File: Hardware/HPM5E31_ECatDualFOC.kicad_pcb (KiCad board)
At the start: 4 copper layers, 85 x 113.4 mm, 403 parts, among them J1 Conn_Coaxial, J11 PHB2.0-02-20PWZ, J12 PHB2.0-02-20PWZ, J13 RJ45_Hanrun_HR911105A_Horizon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, J14 RJ45_Hanrun_HR911105A_Horizon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, J15 WAFER-GH1.25-4PWB, J16 WAFER-GH1.25-4PWB, J17 WAFER-GH1.25-4PWB, J18 WAFER-GH1.25-2PWB, J19 WAFER-GH1.25-2PWB, J2 WAFER-ZH1.5-4PWB, J20 Conn_Coaxial, J3 Conn_02x05_Odd_Even, J4 USB_B, K1 DSHP02TSGET, Q1 CSD19532Q5B, Q10 CSD19532Q5B, Q11 CSD19532Q5B, Q12 CSD19532Q5B, Q13 NCE01ND03S, Q14 NCE01ND03S, Q15 SI2305, Q16 SI2305, Q17 SS8050, Q18 SS8050, Q2 CSD19532Q5B, Q3 CSD19532Q5B, Q4 CSD19532Q5B, Q5 CSD19532Q5B, Q6 CSD19532Q5B, Q7 CSD19532Q5B, Q8 CSD19532Q5B, Q9 CSD19532Q5B, U1 HPM5E31IGN1, U10 UCC27282DRCR, U11 INA240A1PWR, U12 UCC27282DRCR, U13 INA240A1PWR, U14 UCC27282DRCR, U15 INA240A1PWR, U16 INA240A1PWR, U17 UCC27282DRCR, U18 INA240A1PWR, U19 UCC27282DRCR, U2 LM5164DDAR, U20 INA240A1PWR, U21 UCC27282DRCR, U22 INA240A1PWR, U23 INA240A1PWR, U24 PY32F002BF15U, U25 EG2104, U26 ZX-HY2.0-2PWT, U27 RT9193-33GB-MS, U28 EG2104, U29 ZX-HY2.0-2PWT, U3 MP1605GTF-Z, U30 RS622XTDE8, U31 MS2575T, U32 TXB0104RUTR, U33 MS2575T, U34 M3, U35 MS2575T, U36 TXB0104RUTR, U37 MS2575T, U38 M3, U39 JL1111-N032I, U40 JL1111-N032I, U41 SP3485EN-L/TR, U42 SP3485EN-L/TR, U43 SP3485EN-L/TR, U44 TJA1042TK/3, U45 TJA1042TK/3, U46 M3, U47 M3, U5 JW5026, U6 MP1605GTF-Z, U7 LP5907MFX-3.3/NOPB, U8 REF3030AIDBZR, U9 MX25L12833FM2I-10G, X1 24M,10ppm

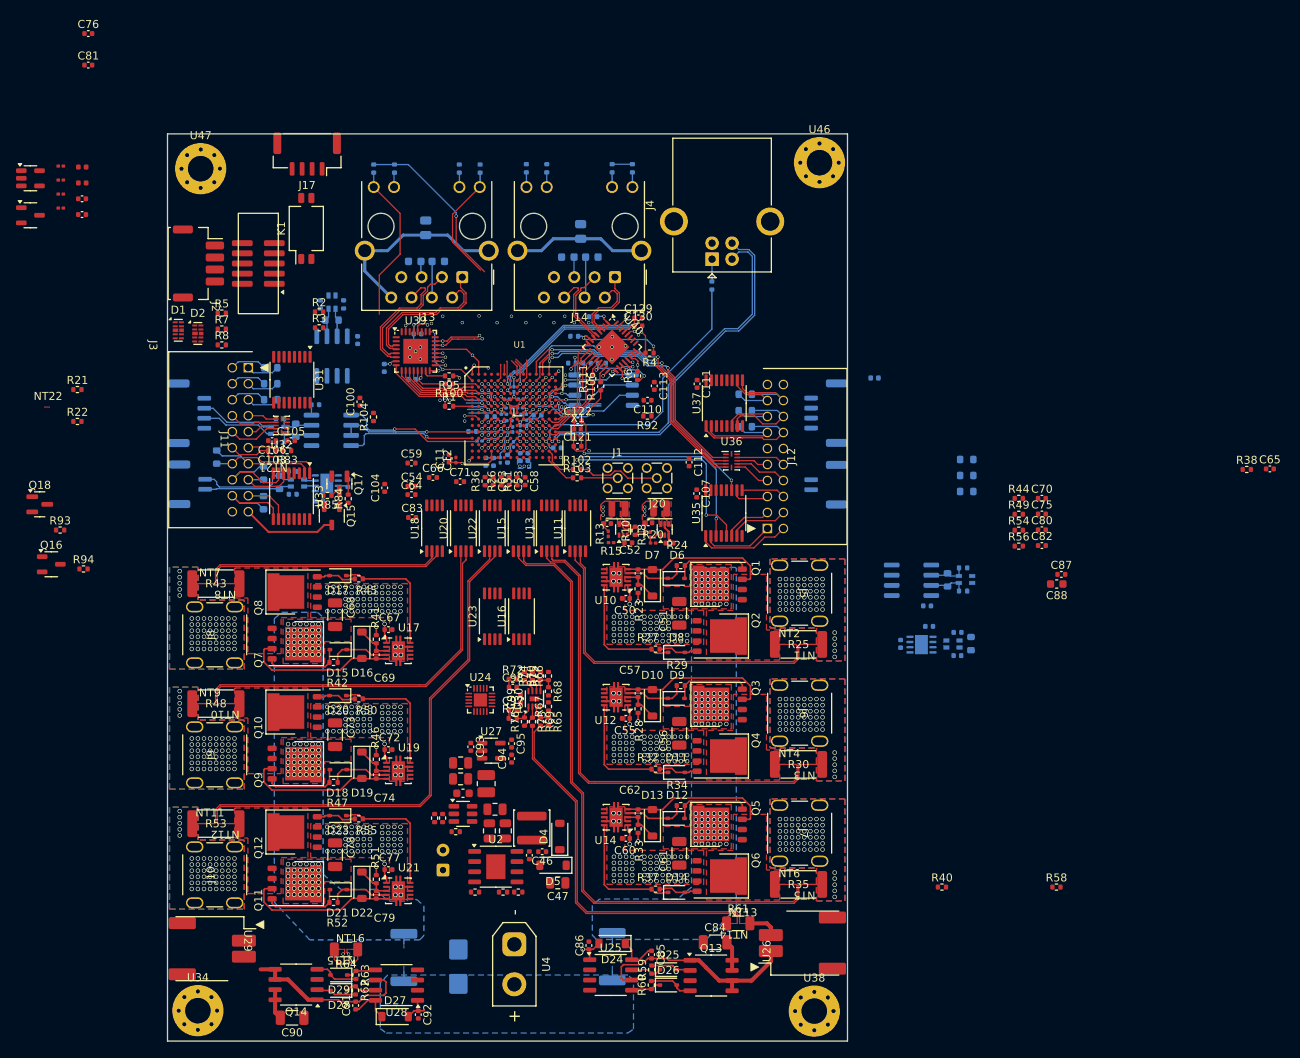
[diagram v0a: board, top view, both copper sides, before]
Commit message: 调整引脚，拉线
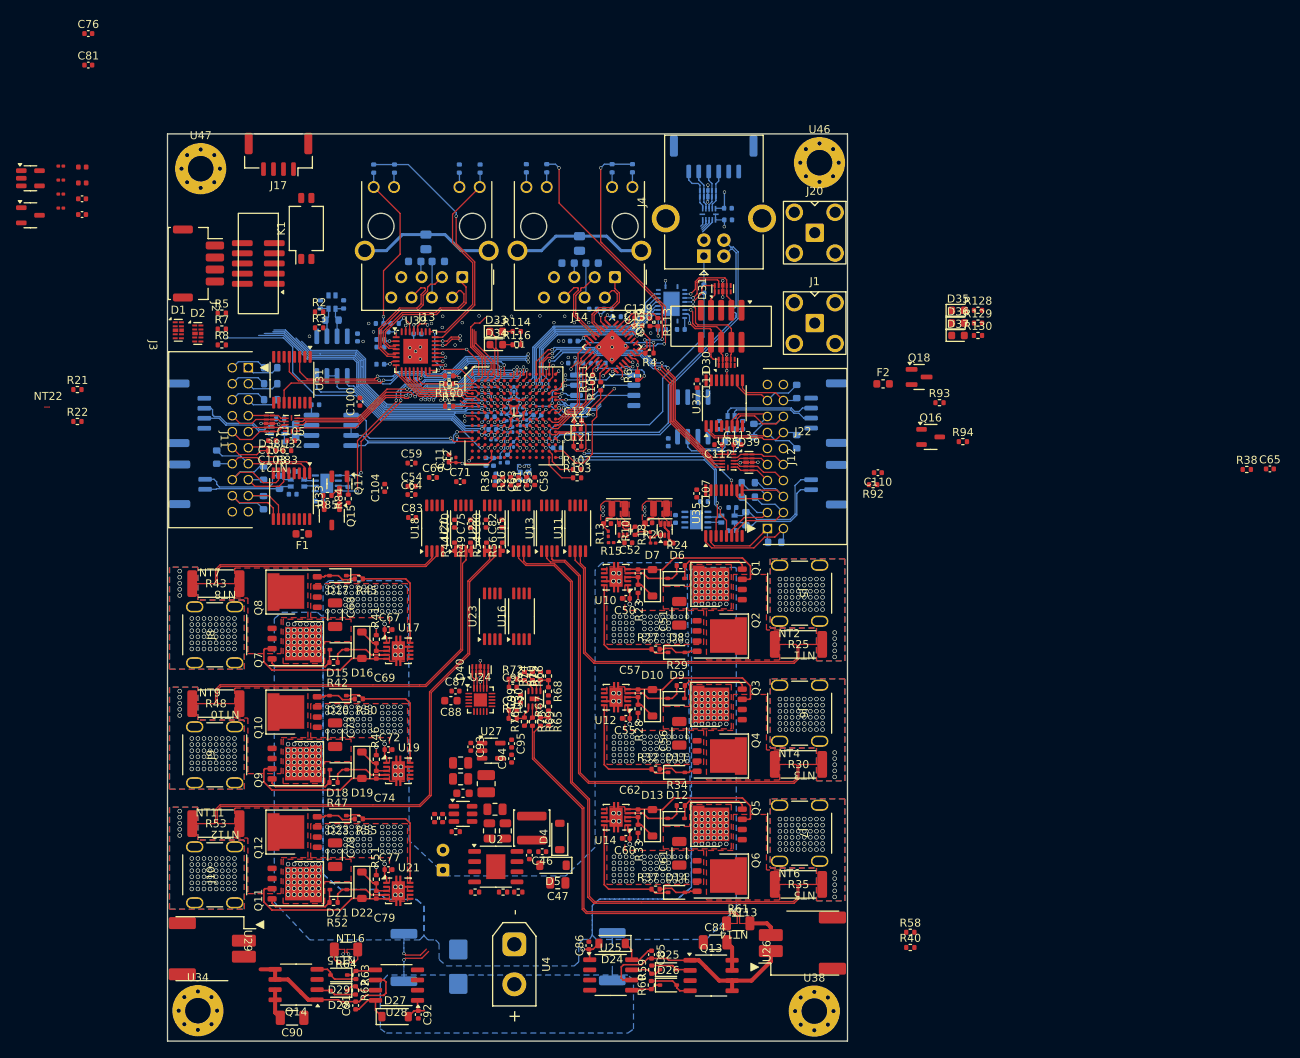
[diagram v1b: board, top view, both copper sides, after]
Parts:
- added C101: 100nF,16V, Capacitor_SMD:C_0402_1005Metric, B.Cu at (88.4, 98.2)
- added C102: 100nF,16V, Capacitor_SMD:C_0402_1005Metric, B.Cu at (116.1, 98.0)
- added C108: 100nF,16V, Capacitor_SMD:C_0402_1005Metric, B.Cu at (88.3, 93.0)
- added C109: 100nF,16V, Capacitor_SMD:C_0402_1005Metric, F.Cu at (122.1, 92.9)
- added C116: 100nF,16V, Capacitor_SMD:C_0402_1005Metric, B.Cu at (131.8, 78.7)
- added C117: 100nF,16V, Capacitor_SMD:C_0402_1005Metric, B.Cu at (123.6, 93.8)
- added C2: 10uF,10V, Capacitor_SMD:C_0402_1005Metric, B.Cu at (88.4, 96.0)
- added C27: 100nF,16V, Capacitor_SMD:C_0402_1005Metric, B.Cu at (88.4, 95.0)
- added C89: 10uF,10V, Capacitor_SMD:C_0402_1005Metric, B.Cu at (115.0, 91.2)
- added C96: 100nF,16V, Capacitor_SMD:C_0402_1005Metric, B.Cu at (116.8, 91.2)
- added D30: RCLAMP0524P, Package_DFN_QFN:Diodes_UDFN-10_1.0x2.5mm_P0.5mm, F.Cu at (131.7, 97.9)
- added D31: RCLAMP0524P, Package_DFN_QFN:Diodes_UDFN-10_1.0x2.5mm_P0.5mm, F.Cu at (131.2, 88.7)
- added D32: RCLAMP0524P, Package_DFN_QFN:Diodes_UDFN-10_1.0x2.5mm_P0.5mm, B.Cu at (129.3, 76.8)
- added D33: NCD0603G1, LED_SMD:LED_0603_1608Metric, F.Cu at (102.9, 94.0)
- added D34: NCD0603R1, LED_SMD:LED_0603_1608Metric, F.Cu at (102.9, 95.7)
- added D35: NCD0603G1, LED_SMD:LED_0603_1608Metric, F.Cu at (160.6, 91.4)
- added D36: NCD0603R1, LED_SMD:LED_0603_1608Metric, F.Cu at (160.6, 93.0)
- added D37: NCD0603B1, LED_SMD:LED_0603_1608Metric, F.Cu at (160.6, 94.5)
- added D38: RCLAMP0524P, Package_DFN_QFN:Diodes_UDFN-10_1.0x2.5mm_P0.5mm, F.Cu at (74.5, 105.5)
- added D39: RCLAMP0524P, Package_DFN_QFN:Diodes_UDFN-10_1.0x2.5mm_P0.5mm, F.Cu at (134.5, 110.4)
- added D40: RCLAMP3324P, Package_DFN_QFN:Diodes_UDFN-10_1.0x2.5mm_P0.5mm, F.Cu at (100.9, 136.3)
- added F1: SMD0603-050-6, Fuse:Fuse_0603_1608Metric, F.Cu at (78.7, 119.3)
- added F2: SMD0603-050-6, Fuse:Fuse_0603_1608Metric, F.Cu at (151.2, 100.6)
- added J21: WAFER-GH1.25-6PWB, Library:JST_GH_SM06B-GHS-TB_1x06-1MP_P1.25mm_Horizontal, B.Cu at (130.1, 72.2)
- added J22: Conn_02x05_Odd_Even, Library:IDC_SMD_P1.27mm_02x05, F.Cu at (131.0, 93.4)
- added R105: 0R,1%, Resistor_SMD:R_0402_1005Metric, B.Cu at (90.2, 93.0)
- added R113: 0R,1%, Resistor_SMD:R_0402_1005Metric, F.Cu at (123.1, 92.9)
- added R114: 2K,1%, Resistor_SMD:R_0402_1005Metric, F.Cu at (105.4, 94.0)
- added R116: 2K,1%, Resistor_SMD:R_0402_1005Metric, F.Cu at (105.4, 95.7)
- added R128: 2K,1%, Resistor_SMD:R_0402_1005Metric, F.Cu at (163.1, 91.4)
- added R129: 2K,1%, Resistor_SMD:R_0402_1005Metric, F.Cu at (163.1, 93.0)
- added R130: 2K,1%, Resistor_SMD:R_0402_1005Metric, F.Cu at (163.1, 94.5)
- added U48: TXB0104RUTR, Library:UQFN-12_1.7x2_Pitch0.4mm, B.Cu at (129.5, 79.4)
- added U49: TXS0108ERGYR, Package_DFN_QFN:Texas_RGY_R-PVQFN-N20_EP2.05x3.05mm, B.Cu at (124.8, 90.6)
- C114, C124: value 10uF,10V -> 100nF,16V
- J1, J20: footprint Connector_Coaxial:MMCX_Molex_73415-1471_Vertical -> Connector_Coaxial:SMA_BAT_Wireless_BWSMA-KWE-Z001
- J4: footprint Connector_USB:USB_B_OST_USB-B1HSxx_Horizontal -> Library:USB_B_OST_USB-B1HSxx_Horizontal
- R104: moved to B.Cu
- moved R93 111.1 mm to (158.3, 103.0)
- moved Q18 111.1 mm to (155.8, 99.7)
- moved Q16 111.1 mm to (157.2, 107.2)
- moved R94 111.1 mm to (161.2, 107.8)
- moved C88 77.1 mm to (97.2, 140.2)
- moved C87 77.1 mm to (97.8, 139.0)
- moved C70 73.5 mm to (97.7, 118.1), turned to 90 degrees
- moved C75 71.5 mm to (99.7, 118.1), turned to 90 degrees
- moved R44 70.8 mm to (97.7, 121.0), turned to 90 degrees
- moved C80 69.5 mm to (101.6, 118.1), turned to 90 degrees
- moved R49 68.7 mm to (99.7, 121.0), turned to 90 degrees
- moved C82 67.6 mm to (103.6, 118.1), turned to 90 degrees
- moved R54 66.6 mm to (101.7, 121.0), turned to 90 degrees
- moved R56 64.6 mm to (103.7, 121.0), turned to 90 degrees
- moved FB1 48.9 mm to (102.8, 112.3), turned to 90 degrees
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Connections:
- net /HPM5E31_TOP/PA0 renamed PA0
- net /HPM5E31_TOP/PA1 renamed PA1
- net /HPM5E31_TOP/PA16 renamed /HPM5E31_TOP/RS485_4.DI
- net /HPM5E31_TOP/PA17 renamed /HPM5E31_TOP/RS485_4.RO
- net /HPM5E31_TOP/PA18 renamed /HPM5E31_TOP/RS485_4.DE
- net /HPM5E31_TOP/PA19 renamed PA19
- net /HPM5E31_TOP/PA2 renamed PA2
- net /HPM5E31_TOP/PA20 renamed PA20
- net /HPM5E31_TOP/PA21 renamed PA21
- net /HPM5E31_TOP/PA22 renamed PA22
- net /HPM5E31_TOP/PA27 renamed PA27
- net /HPM5E31_TOP/PA29 renamed PA29
- net /HPM5E31_TOP/PA3 renamed PA3
- net /HPM5E31_TOP/PA4 renamed PA4
- net /HPM5E31_TOP/PA5 renamed PA5
- net /HPM5E31_TOP/PA6 renamed PA6
- net /HPM5E31_TOP/PA7 renamed PA7
- net /HPM5E31_TOP/PA8 renamed PA8
- net /HPM5E31_TOP/PA9 renamed PA9
- net /HPM5E31_TOP/PC0 renamed /HPM5E31_TOP/CAN0.TXD
- net /HPM5E31_TOP/PC1 renamed /HPM5E31_TOP/CAN0.RXD
- net /HPM5E31_TOP/PC16 renamed PC16
- net /HPM5E31_TOP/PC24 renamed PC24
- net /HPM5E31_TOP/PC25 renamed PC25
- net /HPM5E31_TOP/PC26 renamed /HPM5E31_TOP/FLASH.SCLK
- net /HPM5E31_TOP/PC27 renamed /HPM5E31_TOP/FLASH.CS0
- net /HPM5E31_TOP/PC28 renamed /HPM5E31_TOP/FLASH.D1
- net /HPM5E31_TOP/PC29 renamed /HPM5E31_TOP/FLASH.D0
- net /HPM5E31_TOP/PC3 renamed PC3
- net /HPM5E31_TOP/PC30 renamed /HPM5E31_TOP/FLASH.D2
- net /HPM5E31_TOP/PC31 renamed /HPM5E31_TOP/FLASH.D3
- net /HPM5E31_TOP/PD0 renamed PD0
- net /HPM5E31_TOP/PD10 renamed PD10
- net /HPM5E31_TOP/PD11 renamed PD11
- net /HPM5E31_TOP/PD12 renamed PD12
- net /HPM5E31_TOP/PD13 renamed PD13
- net /HPM5E31_TOP/PD8 renamed PD8
- net /HPM5E31_TOP/PE0 renamed PE0
- net /HPM5E31_TOP/PE1 renamed PE1
- net /HPM5E31_TOP/PE2 renamed PE2
- net /HPM5E31_TOP/PE4 renamed PE4
- net /HPM5E31_TOP/PE5 renamed PE5
- net /HPM5E31_TOP/PF0 renamed /HPM5E31_TOP/DRIVER_A.HI0
- net /HPM5E31_TOP/PF1 renamed /HPM5E31_TOP/DRIVER_A.LI0
- net /HPM5E31_TOP/PF10 renamed /HPM5E31_TOP/DRIVER_B.HI1
- net /HPM5E31_TOP/PF11 renamed /HPM5E31_TOP/DRIVER_B.LI1
- net /HPM5E31_TOP/PF12 renamed /HPM5E31_TOP/DRIVER_B.HI2
- net /HPM5E31_TOP/PF13 renamed /HPM5E31_TOP/DRIVER_B.LI2
- net /HPM5E31_TOP/PF14 renamed PF14
- net /HPM5E31_TOP/PF15 renamed PF15
- net /HPM5E31_TOP/PF19 renamed PF19
- net /HPM5E31_TOP/PF2 renamed /HPM5E31_TOP/DRIVER_A.HI1
- net /HPM5E31_TOP/PF20 renamed /HPM5E31_TOP/DRIVER_A.CUR2
- net /HPM5E31_TOP/PF21 renamed PF21
- net /HPM5E31_TOP/PF23 renamed PF23
- net /HPM5E31_TOP/PF24 renamed PF24
- net /HPM5E31_TOP/PF25 renamed PF25
- net /HPM5E31_TOP/PF26 renamed /HPM5E31_TOP/DRIVER_A.CUR3
- net /HPM5E31_TOP/PF27 renamed PF27
- net /HPM5E31_TOP/PF28 renamed /HPM5E31_TOP/DRIVER_A.CUR1
- net /HPM5E31_TOP/PF29 renamed PF29
- net /HPM5E31_TOP/PF3 renamed /HPM5E31_TOP/DRIVER_A.LI1
- net /HPM5E31_TOP/PF30 renamed PF30
- net /HPM5E31_TOP/PF31 renamed /HPM5E31_TOP/DRIVER_A.CUR0
- net /HPM5E31_TOP/PF4 renamed /HPM5E31_TOP/DRIVER_A.HI2
- net /HPM5E31_TOP/PF5 renamed /HPM5E31_TOP/DRIVER_A.LI2
- net /HPM5E31_TOP/PF6 renamed PF6
- net /HPM5E31_TOP/PF7 renamed PF7
- net /HPM5E31_TOP/PF8 renamed /HPM5E31_TOP/DRIVER_B.HI0
- net /HPM5E31_TOP/PF9 renamed /HPM5E31_TOP/DRIVER_B.LI0
- C124 pad 1: +3.3V -> +5V
- Q15 pad 3: /ENCODER_CONN_A/ENC_PWR -> Net-(Q15-D)
- Q16 pad 3: /ENCODER_CONN_B/ENC_PWR -> Net-(Q16-D)
- U1 pad A10: /HPM5E31_TOP/PC18 -> PC18
- U1 pad A3: /HPM5E31_TOP/PB26 -> PB26
- U1 pad A4: /HPM5E31_TOP/PB28 -> PB28
- U1 pad A5: /HPM5E31_TOP/PB30 -> PB30
- U1 pad A8: /ENCODER_CONN_A/ENC.Z -> /ENCODER_CONN_A/ENC.CS
- U1 pad A9: /ENCODER_CONN_A/ENC.A -> /ENCODER_CONN_A/ENC.MOSI
- U1 pad B10: /HPM5E31_TOP/PC19 -> PC19
- U1 pad B12: /HPM5E31_TOP/PD5 -> /ENCODER_CONN_A/ENC.Z
- U1 pad B13: /HPM5E31_TOP/PD7 -> /ENCODER_CONN_A/ENC.A
- U1 pad B2: /HPM5E31_TOP/PB27 -> PB27
- U1 pad B3: /HPM5E31_TOP/PB29 -> PB29
- U1 pad B4: /HPM5E31_TOP/PB31 -> PB31
- U1 pad B6: /HPM5E31_TOP/PC2 -> PC2
- U1 pad B7: /HPM5E31_TOP/PC4 -> /ENCODER_CONN_A/ENC.CLK
- U1 pad B8: /ENCODER_CONN_A/ENC.B -> /ENCODER_CONN_A/ENC.MISO
- U1 pad B9: /HPM5E31_TOP/PC8 -> PC8
- U1 pad C10: /HPM5E31_TOP/PD1 -> PD1
- U1 pad C11: /HPM5E31_TOP/PD3 -> PD3
- U1 pad C12: /HPM5E31_TOP/PD6 -> /ENCODER_CONN_A/ENC.B
- U1 pad C5: /HPM5E31_TOP/PC9 -> PC9
- U1 pad C6: /ENCODER_CONN_A/ENC.MOSI -> PC11
- U1 pad C7: /ENCODER_CONN_A/ENC.CS -> /HPM5E31_TOP/RS485_3.DE
- U1 pad C8: /HPM5E31_TOP/PC15 -> /HPM5E31_TOP/RS485_3.DI
- U1 pad C9: /HPM5E31_TOP/PC17 -> PC17
- U1 pad D10: /HPM5E31_TOP/PD2 -> PD2
- U1 pad D11: /HPM5E31_TOP/PD4 -> PD4
- U1 pad D12: /HPM5E31_TOP/PD9 -> PD9
- U1 pad D5: /ENCODER_CONN_A/ENC.CLK -> PC10
- U1 pad D6: /ENCODER_CONN_A/ENC.MISO -> PC12
- U1 pad D7: /HPM5E31_TOP/PC14 -> /HPM5E31_TOP/RS485_3.RO
- U1 pad G13: /HPM5E31_TOP/PD15 -> /HPM5E31_TOP/CAN3.TXD
- U1 pad G14: /HPM5E31_TOP/PD14 -> /HPM5E31_TOP/CAN3.RXD
- U1 pad J3: /HPM5E31_TOP/PA26 -> /HPM5E31_TOP/RS485_6.DE
- U1 pad J5: /ETHERNET_PHY_P2/MII.LINK -> PA28
- U1 pad K3: /HPM5E31_TOP/PA24 -> /HPM5E31_TOP/RS485_6.DI
- U1 pad K4: /HPM5E31_TOP/PA25 -> /HPM5E31_TOP/RS485_6.RO
- U1 pad N14: /HPM5E31_TOP/PE3 -> /ETHERNET_PHY_P2/MII.LINK
- U1 pad N7: /HPM5E31_TOP/PF16 -> /HPM5E31_TOP/DRIVER_B.CUR0
- U1 pad N8: /HPM5E31_TOP/PF22 -> /HPM5E31_TOP/DRIVER_B.CUR2
- U1 pad P7: /HPM5E31_TOP/PF17 -> /HPM5E31_TOP/DRIVER_B.CUR1
- U1 pad P8: /HPM5E31_TOP/PF18 -> /HPM5E31_TOP/DRIVER_B.CUR3
- U24 pad 1: /BREAK_MCU/PY32_RST -> PC2
- U24 pad 10: /BREAK_MCU/PY32_INT1 -> PC12
- U24 pad 7: /BREAK_MCU/PY32_RX -> PC8
- U24 pad 8: /BREAK_MCU/PY32_TX -> PC9
- U24 pad 9: /BREAK_MCU/PY32_INT0 -> PC11
- U39 pad 2: unconnected-(U39-REFCLK_SEL-Pad2) -> Net-(U39-REFCLK_SEL)
- U39 pad 30: unconnected-(U39-EN_DLDO-Pad30) -> Net-(U39-EN_DLDO)
- U40 pad 2: unconnected-(U40-REFCLK_SEL-Pad2) -> Net-(U40-REFCLK_SEL)
- U40 pad 30: unconnected-(U40-EN_DLDO-Pad30) -> Net-(U40-EN_DLDO)
- U42 pad 1: /HPM5E31_TOP/PA25 -> /HPM5E31_TOP/RS485_3.RO
- U42 pad 2: /HPM5E31_TOP/PA26 -> /HPM5E31_TOP/RS485_3.DE
- U42 pad 3: /HPM5E31_TOP/PA26 -> /HPM5E31_TOP/RS485_3.DE
- U42 pad 4: /HPM5E31_TOP/PA24 -> /HPM5E31_TOP/RS485_3.DI
- U43 pad 1: /HPM5E31_TOP/RS485_7.RO -> /HPM5E31_TOP/RS485_6.RO
- U43 pad 2: /HPM5E31_TOP/RS485_7.DE -> /HPM5E31_TOP/RS485_6.DE
- U43 pad 3: /HPM5E31_TOP/RS485_7.DE -> /HPM5E31_TOP/RS485_6.DE
- U43 pad 4: /HPM5E31_TOP/RS485_7.DI -> /HPM5E31_TOP/RS485_6.DI
- U45 pad 1: /HPM5E31_TOP/PC15 -> /HPM5E31_TOP/CAN3.TXD
- U45 pad 4: /HPM5E31_TOP/PC14 -> /HPM5E31_TOP/CAN3.RXD
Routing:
- net GNDPWR: track 14.0 -> 123.6 mm
- net /ETHERNET_PHY_P2/MII.LINK: track 3.11 -> 56.0 mm, vias 1 -> 4
- net /HPM5E31_TOP/~{RESET}: track 0.57 -> 40.1 mm
- net /ENCODER_CONN_A/ENC.Z: track 1.99 -> 38.5 mm, vias 0 -> 3
- net /ENCODER_CONN_A/ENC.A: track 2.29 -> 38.1 mm, vias 0 -> 3
- net /ENCODER_CONN_A/ENC.B: track 2.85 -> 38.7 mm, vias 0 -> 3
- net GND: track 215.1 -> 249.7 mm, vias 44 -> 72
- net /ETHERNET_PHY_P2/LED0: track 0.00 -> 33.4 mm, vias 0 -> 3
- net PA3: track 3.98 -> 36.0 mm
- net /HPM5E31_TOP/CAN0.RXD: track 1.25 -> 33.1 mm, vias 0 -> 3
- net PA1: track 2.37 -> 33.7 mm
- net PA2: track 3.26 -> 33.6 mm
- net PA5: track 2.52 -> 32.6 mm
- net /ENCODER_CONN_A/ENC.MOSI: track 3.57 -> 32.9 mm, vias 1 -> 2
- net /HPM5E31_TOP/CAN0.TXD: track 2.22 -> 31.2 mm, vias 0 -> 3
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- added copper zone on B.Cu, net GNDPWR

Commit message: 拉线
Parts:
- added R131: 0R,1%, Resistor_SMD:R_0805_2012Metric, B.Cu at (102.8, 161.8)
- U4: footprint Connector_AMASS:AMASS_XT30UPB-F_1x02_P5.0mm_Vertical -> Connector_AMASS:AMASS_XT60-M_1x02_P7.20mm_Vertical
- moved C65 45.9 mm to (154.6, 120.4)
- moved R38 45.9 mm to (151.8, 120.5)
- moved R54 12.7 mm to (89.0, 120.8)
- moved R44 12.7 mm to (85.0, 120.8)
- moved R56 12.7 mm to (91.0, 120.8)
- moved C70 12.7 mm to (85.0, 118.9)
- moved C75 12.7 mm to (87.0, 118.9)
- moved C80 12.7 mm to (89.0, 118.9)
- moved C82 12.7 mm to (90.9, 118.9)
- moved R49 12.7 mm to (87.0, 120.8)
- moved C104 10.2 mm to (79.8, 118.2)
- moved C100 6.30 mm to (79.8, 104.6)
- moved R80 6.14 mm to (73.8, 111.6), turned to -90 degrees
- moved R82 5.72 mm to (68.1, 115.9)
- moved R81 4.15 mm to (73.8, 115.9), turned to 90 degrees
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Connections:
- D32 pad 1: /HPM5E31_TOP/HPM5E31_PINMAP_2/EUI_CK -> /HPM5E31_TOP/HPM5E31_PINMAP_2/EUI_DI
- D32 pad 10: /HPM5E31_TOP/HPM5E31_PINMAP_2/EUI_CK -> /HPM5E31_TOP/HPM5E31_PINMAP_2/EUI_DI
- D32 pad 2: /HPM5E31_TOP/HPM5E31_PINMAP_2/EUI_SH -> /HPM5E31_TOP/HPM5E31_PINMAP_2/EUI_DO
- D32 pad 4: /HPM5E31_TOP/HPM5E31_PINMAP_2/EUI_DI -> /HPM5E31_TOP/HPM5E31_PINMAP_2/EUI_CK
- D32 pad 5: /HPM5E31_TOP/HPM5E31_PINMAP_2/EUI_DO -> /HPM5E31_TOP/HPM5E31_PINMAP_2/EUI_SH
- D32 pad 6: /HPM5E31_TOP/HPM5E31_PINMAP_2/EUI_DO -> /HPM5E31_TOP/HPM5E31_PINMAP_2/EUI_SH
- D32 pad 7: /HPM5E31_TOP/HPM5E31_PINMAP_2/EUI_DI -> /HPM5E31_TOP/HPM5E31_PINMAP_2/EUI_CK
- D32 pad 9: /HPM5E31_TOP/HPM5E31_PINMAP_2/EUI_SH -> /HPM5E31_TOP/HPM5E31_PINMAP_2/EUI_DO
- D35 pad 1: PC18 -> PA20
- D36 pad 1: PC19 -> PA21
- D37 pad 1: PD1 -> PA22
- J21 pad 1: /HPM5E31_TOP/HPM5E31_PINMAP_2/EUI_DO -> Net-(J21-Pin_1)
- J21 pad 2: /HPM5E31_TOP/HPM5E31_PINMAP_2/EUI_DI -> Net-(J21-Pin_2)
- J21 pad 3: /HPM5E31_TOP/HPM5E31_PINMAP_2/EUI_SH -> /HPM5E31_TOP/HPM5E31_PINMAP_2/EUI_DO
- J21 pad 4: /HPM5E31_TOP/HPM5E31_PINMAP_2/EUI_CK -> /HPM5E31_TOP/HPM5E31_PINMAP_2/EUI_DI
- R10 pad 1: +3V3 -> +3.3V
- U48 pad 10: /HPM5E31_TOP/HPM5E31_PINMAP_2/EUI_CK -> /HPM5E31_TOP/HPM5E31_PINMAP_2/EUI_DI
- U48 pad 2: PB26 -> PB28
- U48 pad 3: PB27 -> PB29
- U48 pad 4: PB28 -> PB26
- U48 pad 5: PB29 -> PB27
- U48 pad 7: /HPM5E31_TOP/HPM5E31_PINMAP_2/EUI_DO -> Net-(J21-Pin_1)
- U48 pad 8: /HPM5E31_TOP/HPM5E31_PINMAP_2/EUI_DI -> Net-(J21-Pin_2)
- U48 pad 9: /HPM5E31_TOP/HPM5E31_PINMAP_2/EUI_SH -> /HPM5E31_TOP/HPM5E31_PINMAP_2/EUI_DO
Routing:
- net PB29: track 8.44 -> 43.1 mm, vias 0 -> 1
- net PB28: track 7.61 -> 42.0 mm, vias 0 -> 1
- net PB26: track 8.31 -> 42.1 mm, vias 0 -> 1
- net PB27: track 11.5 -> 43.1 mm, vias 0 -> 1
- net PA4: track 2.59 -> 26.8 mm, vias 0 -> 1
- net +3.3V: track 82.4 -> 100.3 mm, vias 21 -> 29
- net /ENCODER_CONN_A/A_N: track 4.60 -> 15.4 mm
- net /ENCODER_CONN_A/A_P: track 4.15 -> 12.8 mm
- net PC12: track 9.84 -> 17.9 mm
- net PC9: track 9.89 -> 18.0 mm
- net PC11: track 11.4 -> 19.4 mm
- net PC8: track 16.4 -> 24.3 mm
- net /ENCODER_CONN_A/B_N: track 4.60 -> 11.3 mm
- net /ENCODER_CONN_A/B_P: track 4.15 -> 9.67 mm
- net /ENCODER_CONN_A/Z_N: track 4.60 -> 8.93 mm
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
